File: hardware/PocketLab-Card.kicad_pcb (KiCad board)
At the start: 4 copper layers, 85.6 x 54 mm, 267 parts, among them J1 USB-C DATA/POWER, J2 microSD, J3 EXTERNAL 400uH LF COIL, J4 PROTECTED 1S LiPo 3.7V, J5 30-PIN 2.54mm DUPONT GRID, J8 ER-OLED0.42-1W 72x40 SSD1306B, Q1 AO3400A IR DRIVER, Q2 CSD16406Q3 DISCHARGE, Q3 CSD16406Q3 CHARGE, SW1 RESET, SW2 BOOT, SW3 UP, SW4 DOWN, SW5 MAIN POWER OFF / ON, SW6 PAIR, SW7 SELECT, U1 ESP32-S3-WROOM-1-N8R2, U10 BMI270 (FULL OPTION), U11 BMP390 (FULL OPTION), U12 PCF8563T, U13 TSOP75338WTR 38kHz, U14 BQ29700DSE, U15 TPS2553DBVR 500mA LIMIT, U16 USBLC6-4SC6Y, U17 TPS22919DCKR LF 5V LOAD SWITCH, U18 TCA9534PWR INTERNAL CONTROL, U19 SRV05-4MR6T1G SD ESD, U2 PN5321A3HN/C106, U20 SN74AHCT1G126DBVR RGB LEVEL S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, U21 SN74LV125ATPWR LF/SPI 3V3-TO-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, U22 SN74LVC1G126DBVR LF 5V-TO-3V3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, U23 ATECC608C-SSHDA-T, U24 SRV05-4MR6T1G J5 BUS ESD, U25 SRV05-4MR6T1G J5 SPI ESD, U3 E07-900MM10S 855-925MHz, U4 HTRC11001T/03EE,11 125kHz, U5 BQ24074RGTR, U6 TPS63070RNMR 3V3, U7 TPS61023DRLR 5V BOOST, U8 MAX17048G+T10, U9 TCA9535PWR, Y301 27.12MHz crystal (pins 2/4 sh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, Y501 4MHz 5V CMOS OSCILLATOR, Y701 32.768kHz CL=7pF

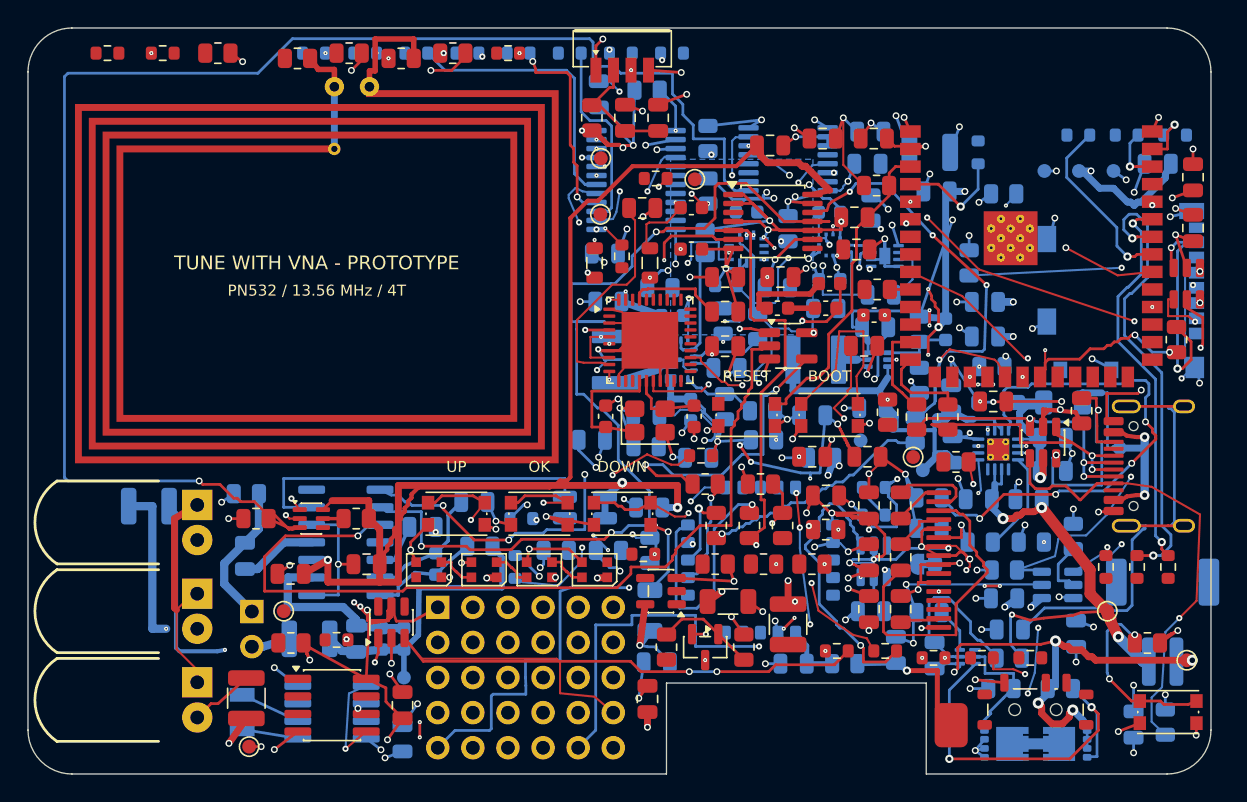
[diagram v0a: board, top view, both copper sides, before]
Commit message: Restore OLED board and close all remaining connections
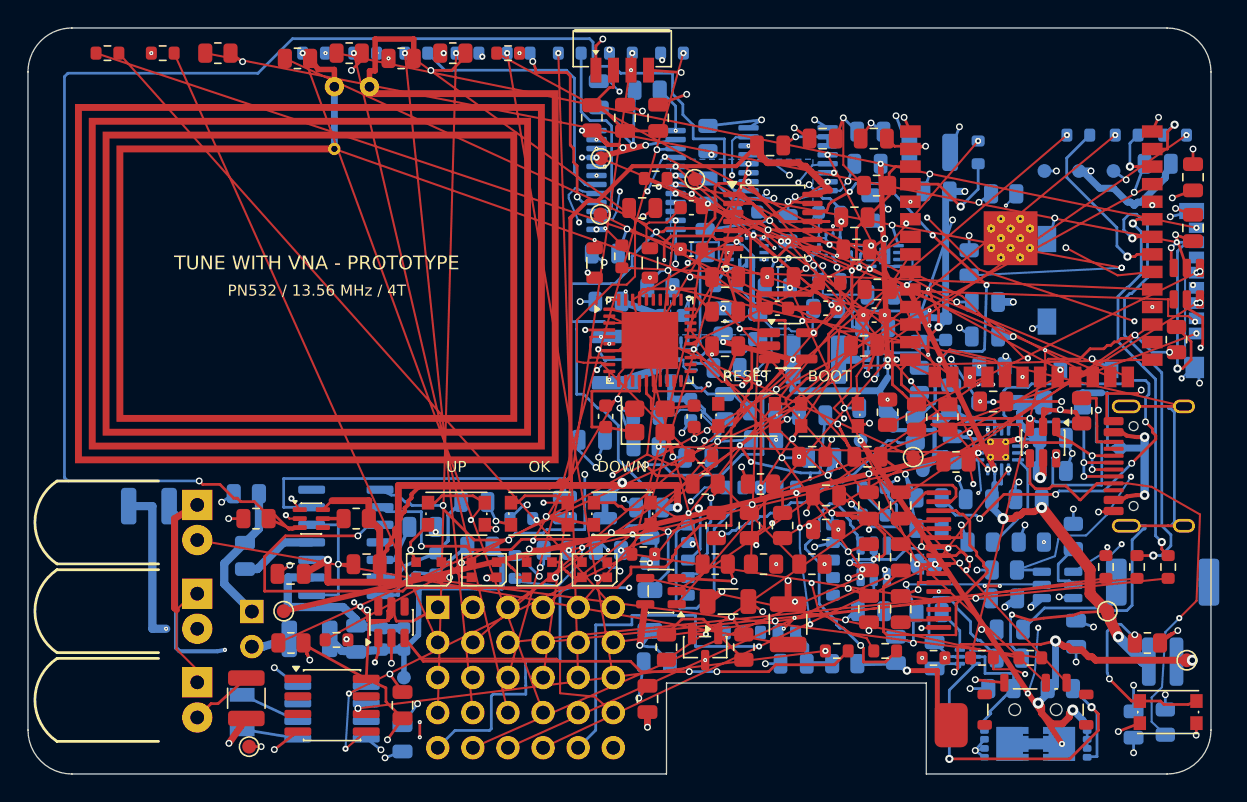
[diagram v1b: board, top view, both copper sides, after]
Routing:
- net /I2C_SDA: track 42.2 -> 120.0 mm, vias 9 -> 13
- net /SD_MISO: track 18.0 -> 89.7 mm, vias 2 -> 3
- net /GPIO43_MCU: track 0.00 -> 68.3 mm
- net /I2C_SCL: track 59.5 -> 124.1 mm, vias 14 -> 18
- net /SD_DAT1: track 0.00 -> 63.5 mm, vias 0 -> 1
- net /BOOT_N: track 13.5 -> 76.0 mm
- net /GPIO8_MCU: track 0.00 -> 62.1 mm
- net /GPIO1: track 0.00 -> 59.8 mm, vias 0 -> 1
- net /GPIO40: track 0.00 -> 56.5 mm, vias 0 -> 1
- net /VBUS_FUSED: track 12.5 -> 67.1 mm, vias 1 -> 2
- net /GPIO8: track 0.00 -> 53.7 mm
- net /GPIO2: track 0.00 -> 53.7 mm, vias 0 -> 1
- net /EX7: track 0.00 -> 50.8 mm, vias 0 -> 1
- net /SD_MOSI: track 0.33 -> 49.8 mm, vias 1 -> 3
- net /NFC_LOOP_A: track 14.3 -> 63.7 mm
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
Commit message: Replace duplicate OLED routing via stacks
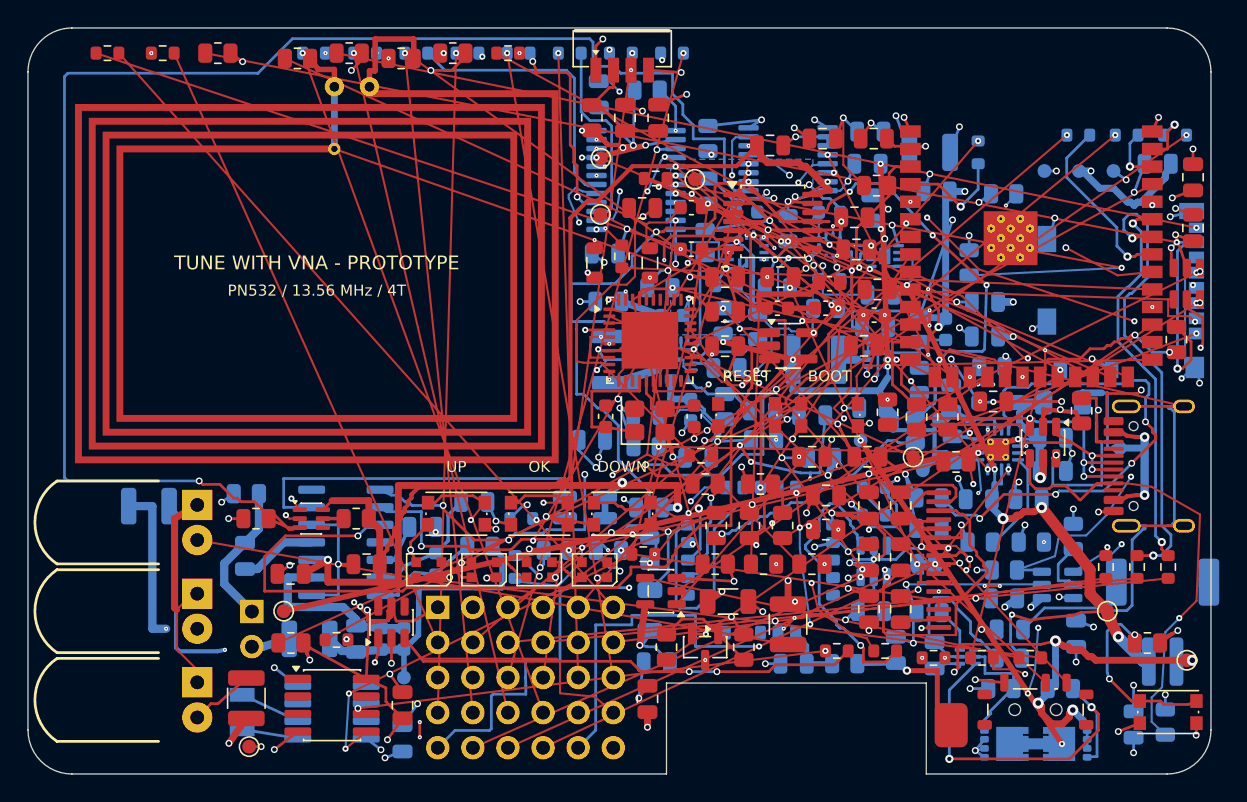
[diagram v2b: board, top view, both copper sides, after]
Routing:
- net /VSYS: vias 8 -> 7
- net /SPI_MOSI_HDR: vias 4 -> 3
- net /I2C_SDA: vias 13 -> 12
- net /I2C_SCL: vias 18 -> 14
- net /CHG_TS: vias 3 -> 2
- net /CHARGER_PGOOD_N: vias 4 -> 3
- net /BQ_EN1: vias 4 -> 3
- net /BOOST5_EN: vias 5 -> 4
- net /AUX5_FAULT_N: vias 4 -> 3
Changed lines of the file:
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@@
 		(net "/BOOST5_EN")
 	)
-	(via micro
-		(at 82.85 44)
-		(size 0.3)
-		(drill 0.1)
-		(layers "In2.Cu" "B.Cu")
-		(locked yes)
-		(net "/BOOST5_EN")
-	)
 	(segment
 		(start 49.915 59.75)
@@
 		(net "/SPI_MOSI_HDR")
 	)
-	(via micro
-		(at 80.25 59.7275)
-		(size 0.3)
-		(drill 0.1)
-		(layers "In2.Cu" "B.Cu")
-		(locked yes)
-		(net "/SPI_MOSI_HDR")
-	)
 	(segment
 		(start 47.9125 20.8)
@@
 		(net "/I2C_SDA")
 	)
-	(via micro
-		(at 72.5 34.9875)
-		(size 0.3)
-		(drill 0.1)
-		(layers "In2.Cu" "B.Cu")
-		(locked yes)
-		(net "/I2C_SDA")
-	)
 	(segment
 		(start 83.85 33.84)
@@
 		(net "/I2C_SCL")
 	)
-	(via micro
-		(at 77.7 65.075)
-		(size 0.3)
-		(drill 0.1)
-		(layers "F.Cu" "In1.Cu")
-		(locked yes)
-		(net "/I2C_SCL")
-	)
 	(via
 		(at 83.55 34.14)
@@
 		(net "/I2C_SCL")
 	)
-	(via micro
-		(at 69.2 32.7125)
-		(size 0.3)
-		(drill 0.1)
-		(layers "In2.Cu" "B.Cu")
-		(locked yes)
-		(net "/I2C_SCL")
-	)
-	(via micro
-		(at 69.2 32.7125)
-		(size 0.3)
-		(drill 0.1)
-		(layers "In2.Cu" "B.Cu")
-		(locked yes)
-		(net "/I2C_SCL")
-	)
 	(segment
 		(start 87.6 39.4)
@@
 	)
 	(via micro
-		(at 70.3 42.7125)
-		(size 0.3)
-		(drill 0.1)
-		(layers "In2.Cu" "B.Cu")
-		(locked yes)
-		(net "/VSYS")
-	)
-	(via micro
 		(at 66.5 42.6)
 		(size 0.3)
@@
 	)
 	(via micro
-		(at 78.6375 40.295)
-		(size 0.3)
-		(drill 0.1)
-		(layers "In2.Cu" "B.Cu")
-		(locked yes)
-		(net "/CHARGER_PGOOD_N")
-	)
-	(via micro
 		(at 88.7625 50.25)
 		(size 0.3)
@@
 	)
 	(via
-		(at 82.85 44)
-		(size 0.45)
-		(drill 0.2)
-		(layers "F.Cu" "B.Cu")
-		(locked yes)
-		(net "/BOOST5_EN")
-	)
-	(via
 		(at 72.1375 31.125)
 		(size 0.45)
@@
 	)
 	(via
-		(at 80.25 59.7275)
-		(size 0.45)
-		(drill 0.2)
-		(layers "F.Cu" "B.Cu")
-		(locked yes)
-		(net "/SPI_MOSI_HDR")
-	)
-	(via
 		(at 91.6375 49.75)
 		(size 0.45)
@@
 	)
 	(via
-		(at 72.5 34.9875)
-		(size 0.45)
-		(drill 0.2)
-		(layers "F.Cu" "B.Cu")
-		(locked yes)
-		(net "/I2C_SDA")
-	)
-	(via
-		(at 69.2 32.7125)
-		(size 0.45)
-		(drill 0.2)
-		(layers "F.Cu" "B.Cu")
-		(locked yes)
-		(net "/I2C_SCL")
-	)
-	(via
-		(at 43.875 69.235)
-		(size 0.45)
-		(drill 0.2)
-		(layers "F.Cu" "B.Cu")
-		(locked yes)
-		(net "/I2C_SCL")
-	)
-	(via
 		(at 80.375 59.175)
 		(size 0.45)
@@
 	)
 	(via
-		(at 77.7 65.075)
-		(size 0.45)
-		(drill 0.2)
-		(layers "F.Cu" "B.Cu")
-		(locked yes)
-		(net "/I2C_SCL")
-	)
-	(via
 		(at 73 53.25)
 		(size 0.45)
@@
 	)
 	(via
-		(at 85.645 58.795)
-		(size 0.45)
-		(drill 0.2)
-		(layers "F.Cu" "B.Cu")
-		(locked yes)
-		(net "/CHG_TS")
-	)
-	(via
 		(at 90.95 51.9375)
 		(size 0.45)
@@
 	)
 	(via
-		(at 70.3 42.7125)
-		(size 0.45)
-		(drill 0.2)
-		(layers "F.Cu" "B.Cu")
-		(locked yes)
-		(net "/VSYS")
-	)
-	(via
 		(at 75.35 44)
 		(size 0.45)
@@
 	)
 	(via
-		(at 88.7625 50.75)
-		(size 0.45)
-		(drill 0.2)
-		(layers "F.Cu" "B.Cu")
-		(locked yes)
-		(net "/BQ_EN1")
-	)
-	(via
-		(at 99.1375 37.35)
-		(size 0.45)
-		(drill 0.2)
-		(layers "F.Cu" "B.Cu")
-		(locked yes)
-		(net "/AUX5_FAULT_N")
-	)
-	(via
 		(at 66.8625 31.325)
 		(size 0.45)
@@
 	)
 	(via
-		(at 78.6375 40.295)
-		(size 0.45)
-		(drill 0.2)
-		(layers "F.Cu" "B.Cu")
-		(locked yes)
-		(net "/CHARGER_PGOOD_N")
-	)
-	(via
 		(at 94.815 71.8)
 		(size 0.45)
@@
 		(net "/CHG_DISABLE")
 	)
+	(via
+		(at 82.85 44)
+		(size 0.45)
+		(drill 0.2)
+		(layers "F.Cu" "B.Cu")
+		(locked yes)
+		(net "/BOOST5_EN")
+	)
+	(via
+		(at 80.25 59.7275)
+		(size 0.45)
+		(drill 0.2)
+		(layers "F.Cu" "B.Cu")
+		(locked yes)
+		(net "/SPI_MOSI_HDR")
+	)
+	(via
+		(at 72.5 34.9875)
+		(size 0.45)
+		(drill 0.2)
+		(layers "F.Cu" "B.Cu")
+		(locked yes)
+		(net "/I2C_SDA")
+	)
+	(via
+		(at 69.2 32.7125)
+		(size 0.45)
+		(drill 0.2)
+		(layers "F.Cu" "B.Cu")
+		(locked yes)
+		(net "/I2C_SCL")
+	)
+	(via
+		(at 77.7 65.075)
+		(size 0.45)
+		(drill 0.2)
+		(layers "F.Cu" "B.Cu")
+		(locked yes)
+		(net "/I2C_SCL")
+	)
+	(via
+		(at 70.3 42.7125)
+		(size 0.45)
+		(drill 0.2)
+		(layers "F.Cu" "B.Cu")
+		(locked yes)
+		(net "/VSYS")
+	)
+	(via
+		(at 78.6375 40.295)
+		(size 0.45)
+		(drill 0.2)
+		(layers "F.Cu" "B.Cu")
+		(locked yes)
+		(net "/CHARGER_PGOOD_N")
+	)
 	(zone

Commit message: Reduce OLED routing drill conflicts
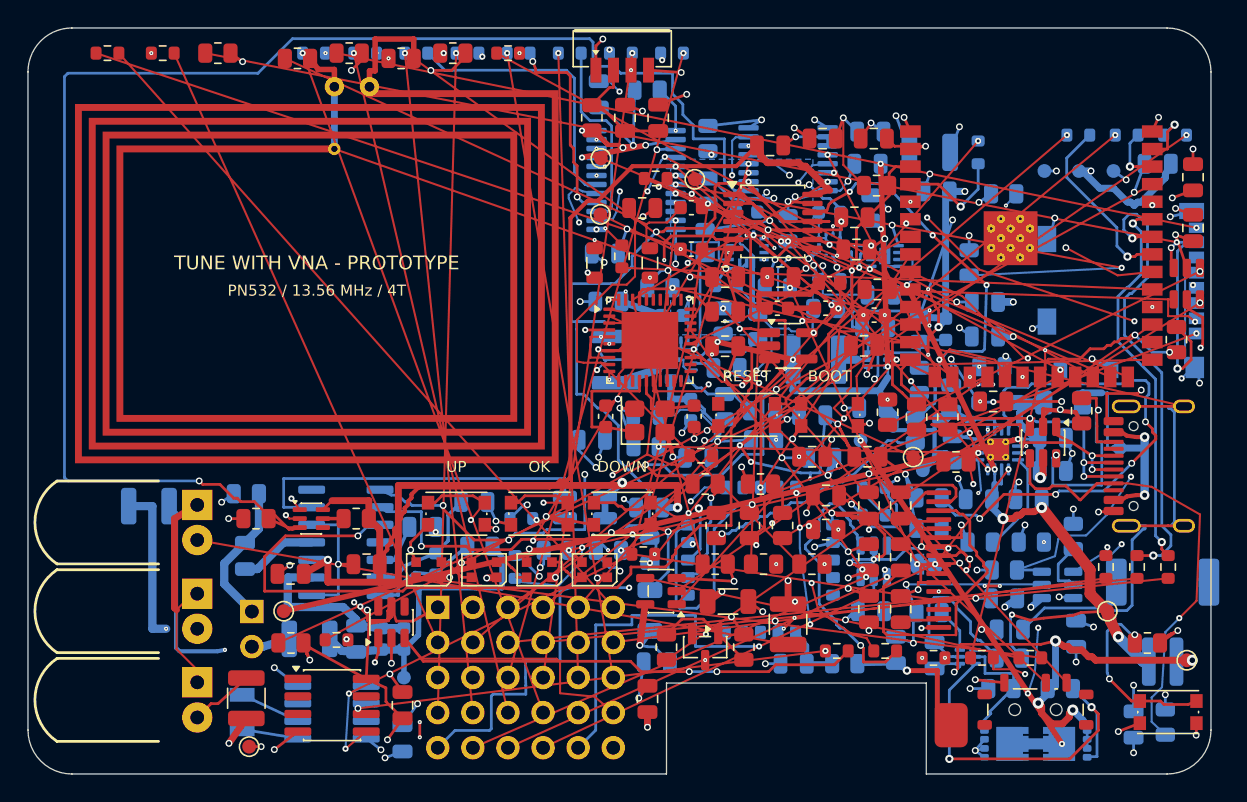
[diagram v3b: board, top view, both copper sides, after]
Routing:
- net /I2C_SDA: track 120.0 -> 122.7 mm, vias 12 -> 11
- net /GND: track 414.4 -> 415.4 mm, vias 146 -> 145
- net /BOOST5_EN: track 48.3 -> 48.7 mm, vias 4 -> 3
- net /SD_SCK: track 25.3 -> 25.5 mm, vias 2 -> 1
- net /SD_MOSI: track 49.8 -> 50.0 mm, vias 3 -> 2
- net /VSYS: track 58.4 -> 58.5 mm, vias 7 -> 6
- net /SPI_MOSI_HDR: vias 3 -> 2
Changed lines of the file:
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@@
 	)
 	(segment
-		(start 61.1375 29.375)
-		(end 60.0875 29.375)
-		(width 0.15)
-		(locked yes)
-		(layer "B.Cu")
-		(net "/GND")
-	)
-	(segment
 		(start 53.25 54.3)
 		(end 53.861782 55.685081)
@@
 	)
 	(segment
-		(start 82.2125 44)
-		(end 82.85 44)
-		(width 0.15)
-		(locked yes)
-		(layer "B.Cu")
-		(net "/BOOST5_EN")
-	)
-	(segment
 		(start 82.85 44)
 		(end 83.3 43)
@@
 		(net "/SPI_MOSI_HDR")
 	)
-	(via micro
-		(at 80.65 59.7275)
-		(size 0.3)
-		(drill 0.1)
-		(layers "In1.Cu" "In2.Cu")
-		(locked yes)
-		(net "/SPI_MOSI_HDR")
-	)
-	(segment
-		(start 80.25 59.7275)
-		(end 80.65 59.7275)
-		(width 0.15)
-		(locked yes)
-		(layer "In2.Cu")
-		(net "/SPI_MOSI_HDR")
-	)
 	(segment
 		(start 47.9125 20.8)
@@
 	(segment
 		(start 70.3 42.1125)
-		(end 70.3 42.7125)
+		(end 69.899999 42.7125)
 		(width 0.15)
 		(locked yes)
@@
 		(net "/VSYS")
 	)
-	(via micro
-		(at 69.899999 42.7125)
-		(size 0.3)
-		(drill 0.1)
-		(layers "In1.Cu" "In2.Cu")
-		(locked yes)
-		(net "/VSYS")
-	)
 	(segment
 		(start 66.5 42.6)
@@
 		(net "/VSYS")
 	)
-	(segment
-		(start 70.3 42.7125)
-		(end 69.899999 42.7125)
-		(width 0.15)
-		(locked yes)
-		(layer "In2.Cu")
-		(net "/VSYS")
-	)
 	(via micro
 		(at 66.5 42.6)
@@
 	(segment
 		(start 64.692803 28.481781)
-		(end 61.1375 29.375)
+		(end 60.0875 29.375)
 		(width 0.4)
 		(locked yes)
@@
 	(segment
 		(start 66.9375 61.7)
-		(end 82.2125 44)
+		(end 82.85 44)
 		(width 0.15)
 		(locked yes)
@@
 	)
 	(segment
-		(start 80.25 59.7275)
+		(start 80.65 59.7275)
 		(end 52.19 72.08)
 		(width 0.15)
@@
 	)
 	(segment
-		(start 104.55 39.905)
+		(start 104.8 39.8875)
 		(end 86.2375 51.4)
 		(width 0.15)
@@
 	(segment
 		(start 82.2 48.7125)
-		(end 104.55 37.705)
+		(end 104.8 37.6125)
 		(width 0.15)
 		(locked yes)
@@
 	)
 	(segment
-		(start 70.3 42.7125)
+		(start 69.899999 42.7125)
 		(end 75.35 44)
 		(width 0.4)
@@
 	)
 	(via
-		(at 61.1375 29.375)
-		(size 0.45)
-		(drill 0.2)
-		(layers "F.Cu" "B.Cu")
-		(locked yes)
-		(net "/GND")
-	)
-	(via
-		(at 82.2125 44)
-		(size 0.45)
-		(drill 0.2)
-		(layers "F.Cu" "B.Cu")
-		(locked yes)
-		(net "/BOOST5_EN")
-	)
-	(via
 		(at 72.1375 31.125)
 		(size 0.45)
@@
 	)
 	(via
-		(at 71.275 35.475)
-		(size 0.45)
-		(drill 0.2)
-		(layers "F.Cu" "B.Cu")
-		(locked yes)
-		(net "/I2C_SDA")
-	)
-	(via
 		(at 81.0125 35.75)
 		(size 0.45)
@@
 	)
 	(via
-		(at 104.55 39.905)
-		(size 0.45)
-		(drill 0.2)
-		(layers "F.Cu" "B.Cu")
-		(locked yes)
-		(net "/SD_MOSI")
-	)
-	(via
 		(at 59.1375 57.795)
 		(size 0.45)
@@
 	)
 	(via
-		(at 104.55 37.705)
-		(size 0.45)
-		(drill 0.2)
-		(layers "F.Cu" "B.Cu")
-		(locked yes)
-		(net "/SD_SCK")
-	)
-	(via
 		(at 103.825 27.75)
 		(size 0.45)
@@
 	)
 	(via
-		(at 80.25 59.7275)
+		(at 80.65 59.7275)
 		(size 0.45)
 		(drill 0.2)
@@
 	)
 	(via
-		(at 70.3 42.7125)
+		(at 69.899999 42.7125)
 		(size 0.45)
 		(drill 0.2)
@@
 		(net "/CHARGER_PGOOD_N")
 	)
+	(segment
+		(start 61.1375 29.375)
+		(end 60.0875 29.375)
+		(width 0.15)
+		(locked yes)
+		(layer "B.Cu")
+		(net "/GND")
+	)
+	(segment
+		(start 71.275 35.475)
+		(end 72.5 34.9875)
+		(width 0.15)
+		(locked yes)
+		(layer "F.Cu")
+		(net "/I2C_SDA")
+	)
+	(segment
+		(start 71.275 35.475)
+		(end 72.5 34.9875)
+		(width 0.15)
+		(locked yes)
+		(layer "In2.Cu")
+		(net "/I2C_SDA")
+	)
+	(segment
+		(start 82.2125 44)
+		(end 82.85 44)
+		(width 0.15)
+		(locked yes)
+		(layer "B.Cu")
+		(net "/BOOST5_EN")
+	)
 	(zone
